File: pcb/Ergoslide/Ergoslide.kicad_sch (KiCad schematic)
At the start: 222 parts, among them J1 Conn_01x02_Socket, J2 Conn_01x02_Socket, SW1 Power Switch

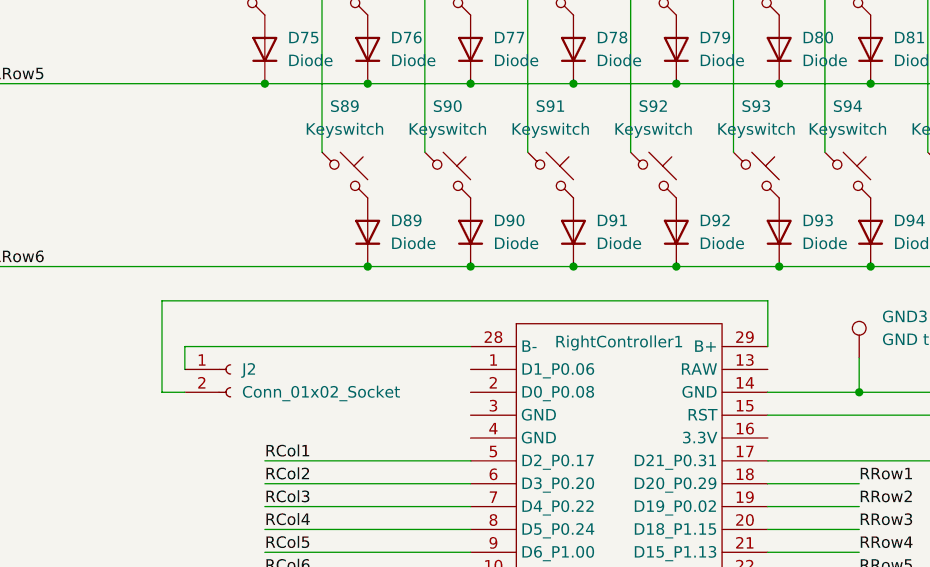
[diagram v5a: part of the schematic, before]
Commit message: Use stabilized switch cutouts
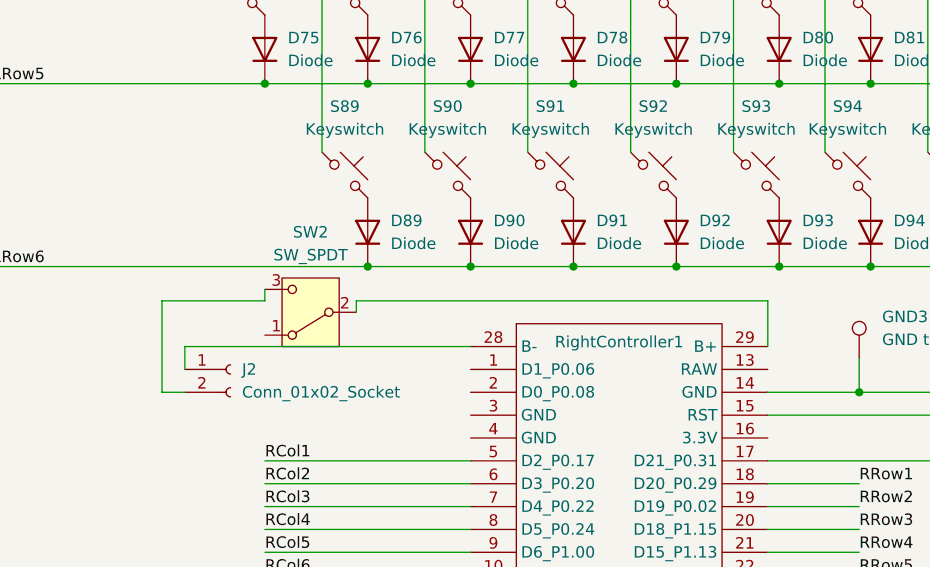
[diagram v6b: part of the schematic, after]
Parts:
- added SW2: SW_SPDT, Button_Switch_SMD:SW_SPDT_CK_JS102011SAQN, symbol Switch:SW_SPDT
- S65, S69, S89: footprint Gateron_KS33_Hotswap:Gateron-KS33-Hotswap-2.25U -> Gateron_KS33_Hotswap:Gateron-KS33-Hotswap-2.25U Stabilized
- S88: footprint Gateron_KS33_Hotswap:Gateron-KS33-Hotswap-2.75U -> Gateron_KS33_Hotswap:Gateron-KS33-Hotswap-2.75U Stabilized
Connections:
- net at RightController1.29 (B+): now also SW2.2 (B); no longer J2.2 (Pin_2)
- new net: J2.2 (Pin_2), SW2.3 (C)
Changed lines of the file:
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@@
 	(wire
 		(pts
+			(xy 267.97 187.96) (xy 267.97 189.23)
+		)
+		(stroke
+			(width 0)
+			(type default)
+		)
+	)
+	(wire
+		(pts
 			(xy 297.18 55.88) (xy 297.18 71.12)
 		)
@@
 	(wire
 		(pts
-			(xy 256.54 189.23) (xy 323.85 189.23)
+			(xy 256.54 189.23) (xy 267.97 189.23)
 		)
 		(stroke
@@
 	(wire
 		(pts
+			(xy 278.13 189.23) (xy 278.13 190.5)
+		)
+		(stroke
+			(width 0)
+			(type default)
+		)
+	)
+	(wire
+		(pts
 			(xy 325.12 165.1) (xy 335.28 165.1)
 		)
@@
 	(wire
 		(pts
+			(xy 278.13 189.23) (xy 323.85 189.23)
+		)
+		(stroke
+			(width 0)
+			(type default)
+		)
+	)
+	(wire
+		(pts
 			(xy 274.32 71.12) (xy 274.32 91.44)
 		)
@@
 			)
 		)
-		(property "Footprint" "Gateron_KS33_Hotswap:Gateron-KS33-Hotswap-2.25U"
+		(property "Footprint" "Gateron_KS33_Hotswap:Gateron-KS33-Hotswap-2.25U Stabilized"
 			(at 332.74 134.62 0)
 			(effects
@@
 			)
 		)
-		(property "Footprint" "Gateron_KS33_Hotswap:Gateron-KS33-Hotswap-2.75U"
+		(property "Footprint" "Gateron_KS33_Hotswap:Gateron-KS33-Hotswap-2.75U Stabilized"
 			(at 129.54 173.99 0)
 			(effects
@@
 	)
 	(symbol
+		(lib_id "Switch:SW_SPDT")
+		(at 273.05 190.5 180)
+		(unit 1)
+		(exclude_from_sim no)
+		(in_bom yes)
+		(on_board yes)
+		(dnp no)
+		(fields_autoplaced yes)
+		(property "Reference" "SW2"
+			(at 273.05 181.61 0)
+			(effects
+				(font
+					(size 1.27 1.27)
+				)
+			)
+		)
+		(property "Value" "SW_SPDT"
+			(at 273.05 184.15 0)
+			(effects
+				(font
+					(size 1.27 1.27)
+				)
+			)
+		)
+		(property "Footprint" "Button_Switch_SMD:SW_SPDT_CK_JS102011SAQN"
+			(at 273.05 190.5 0)
+			(effects
+				(font
+					(size 1.27 1.27)
+				)
+				(hide yes)
+			)
+		)
+		(property "Datasheet" "~"
+			(at 273.05 182.88 0)
+			(effects
+				(font
+					(size 1.27 1.27)
+				)
+				(hide yes)
+			)
+		)
+		(property "Description" "Switch, single pole double throw"
+			(at 273.05 190.5 0)
+			(effects
+				(font
+					(size 1.27 1.27)
+				)
+				(hide yes)
+			)
+		)
+		(pin "2"
+		)
+		(pin "3"
+		)
+		(pin "1"
+		)
+		(instances
+			(project ""
+				(path "/3bd86599-9c29-4fa4-bb71-eb869531a59b"
+					(reference "SW2")
+					(unit 1)
+				)
+			)
+		)
+	)
+	(symbol
 		(lib_id "ScottoKeebs:Placeholder_Keyswitch")
 		(at 332.74 154.94 0)
@@
 			)
 		)
-		(property "Footprint" "Gateron_KS33_Hotswap:Gateron-KS33-Hotswap-2.25U"
+		(property "Footprint" "Gateron_KS33_Hotswap:Gateron-KS33-Hotswap-2.25U Stabilized"
 			(at 276.86 175.26 0)
 			(effects
@@
 			)
 		)
-		(property "Footprint" "Gateron_KS33_Hotswap:Gateron-KS33-Hotswap-2.25U"
+		(property "Footprint" "Gateron_KS33_Hotswap:Gateron-KS33-Hotswap-2.25U Stabilized"
 			(at 95.25 153.67 0)
 			(effects

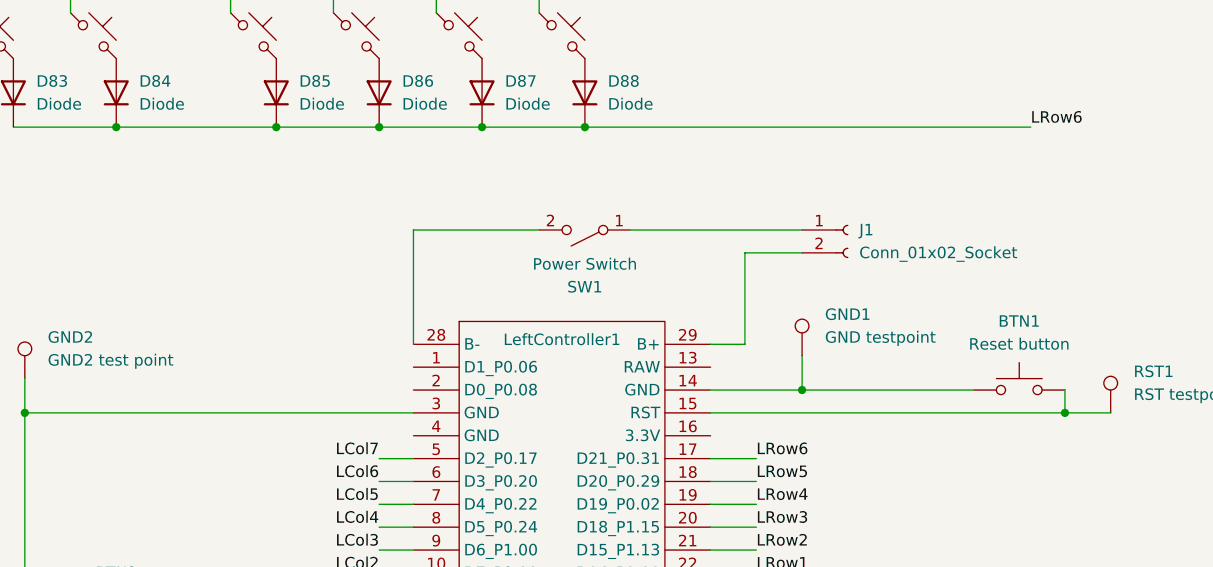
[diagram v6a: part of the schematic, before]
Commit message: Add Caps Lock LED, remove labels for holes, realign labels for everything else
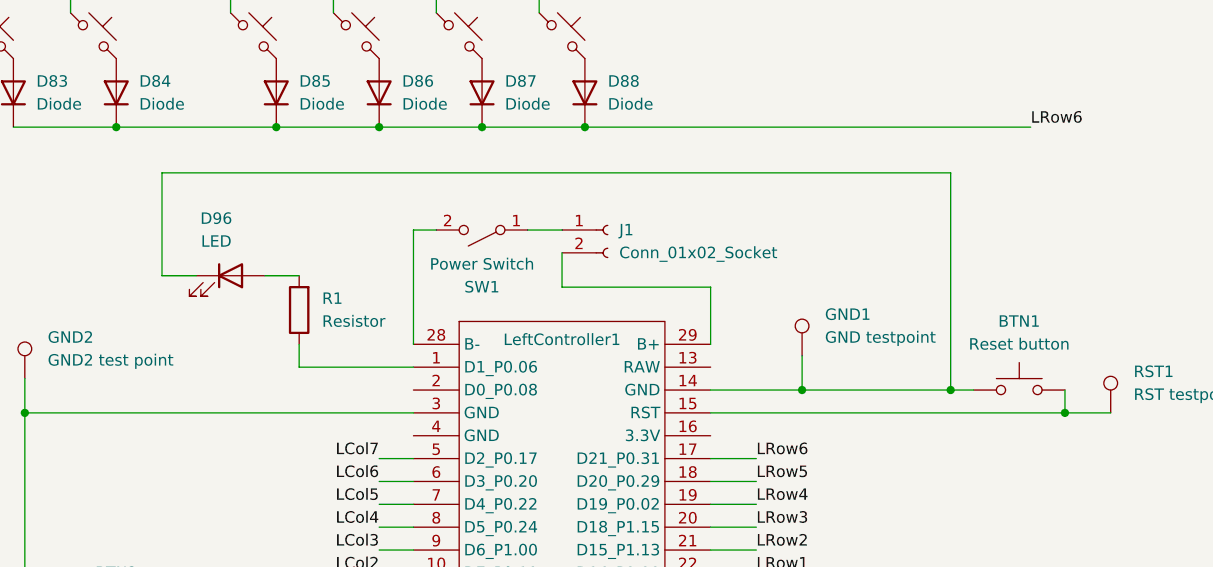
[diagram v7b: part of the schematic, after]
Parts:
- added D96: LED, LED_SMD:LED_0603_1608Metric, symbol Device:LED
- added R1: Resistor, Resistor_SMD:R_0603_1608Metric, symbol ScottoKeebs:Placeholder_Resistor
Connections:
- net at BTN1.1, GND1.1, LeftController1.14 (GND): now also D96.1 (K)
- net at LeftController1.1 (D1_P0.06): now also R1.1
- new net: D96.2 (A), R1.2
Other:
- moved on the sheet: J1, SW1
